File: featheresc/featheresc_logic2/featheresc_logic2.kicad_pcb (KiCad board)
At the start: 2 copper layers, 77 x 39 mm, 52 parts, among them J1 RC IN 1, J2 RC IN 2, J3 soicbite prog connector, J7 Interconnect 1, J8 Interconnect 2, SW1 SW_DIP_x01, U1 AMS1117-50, U2 XL1509-ADJE1, U3 ATtiny1614-SS, U4 NCP81155MN, U5 NCP81155MN, U6 NCP81155MN, U7 NCP81155MN, U8 78L12G-AB3-R

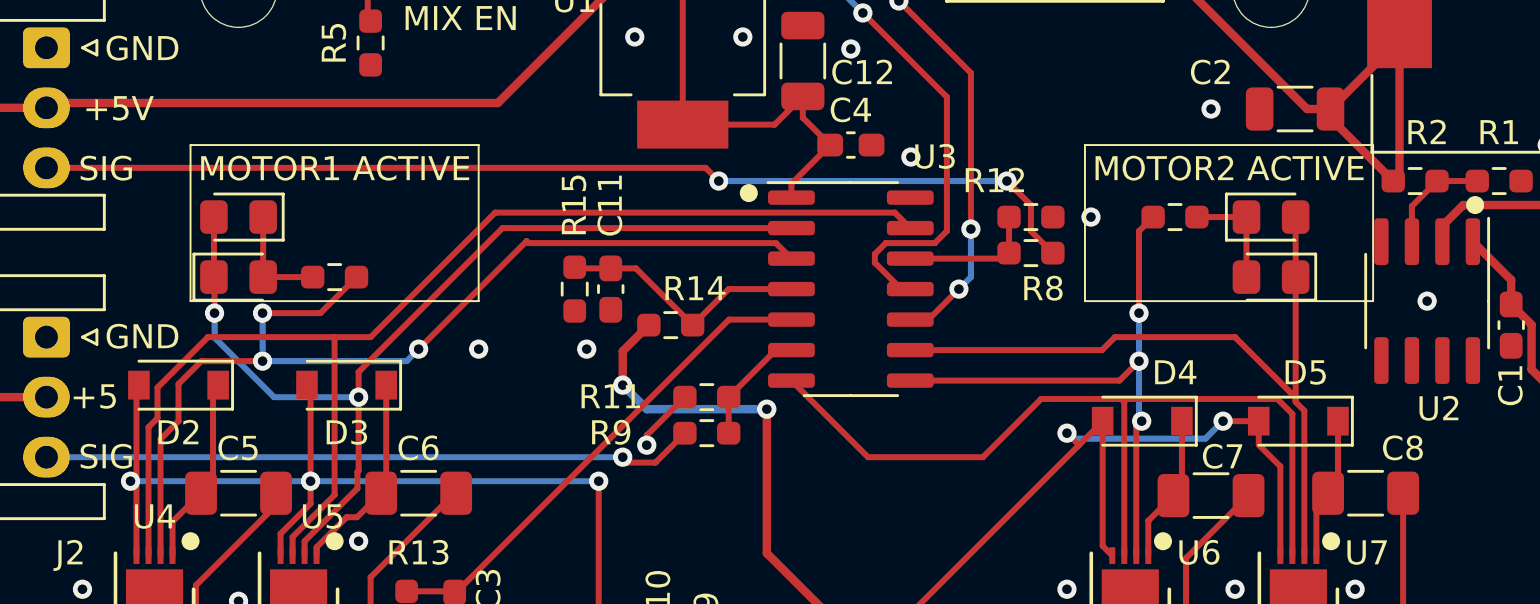
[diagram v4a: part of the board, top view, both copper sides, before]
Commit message: Pulldown EN pins
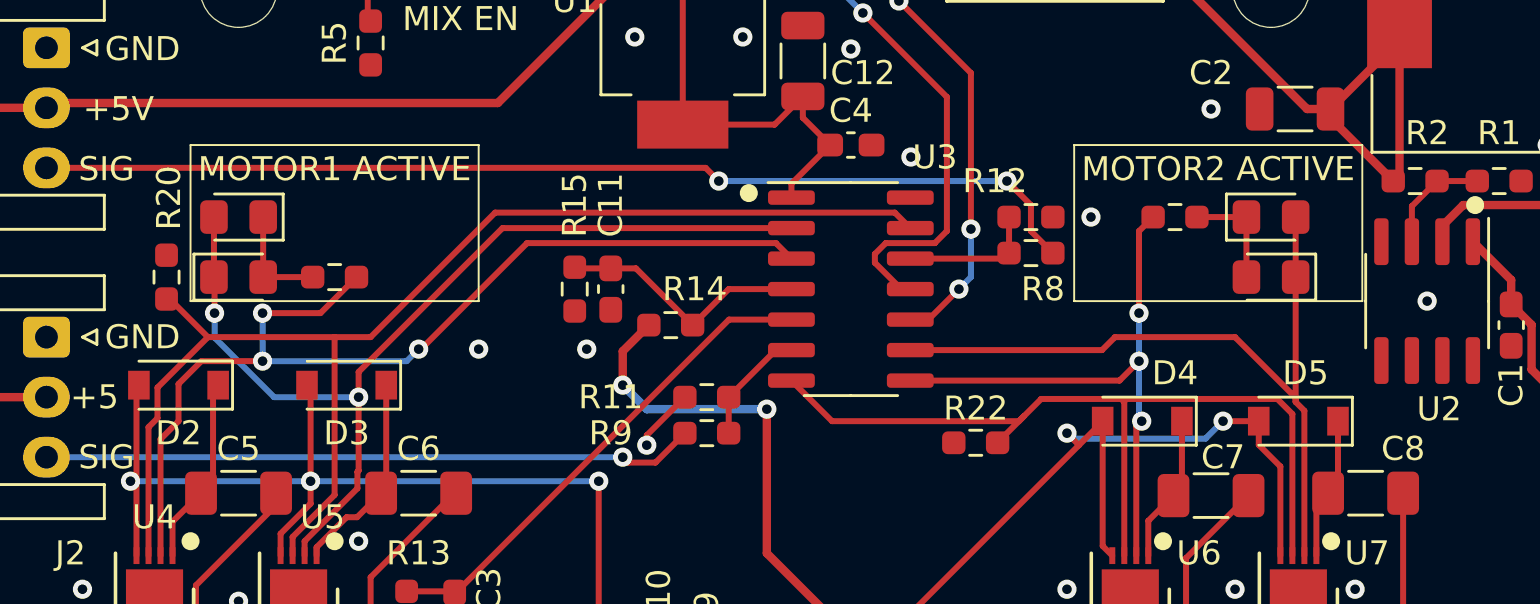
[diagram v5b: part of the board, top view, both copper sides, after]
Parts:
- added R20: 33k, Resistor_SMD:R_0603_1608Metric_Pad0.98x0.95mm_HandSolder, F.Cu at (125.0, 77.0)
- added R22: 33k, Resistor_SMD:R_0603_1608Metric_Pad0.98x0.95mm_HandSolder, F.Cu at (158.7, 83.9)
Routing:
- net /MOTOREN_1: track 51.6 -> 54.0 mm
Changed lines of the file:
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@@
+    )
+  )
+  (footprint "Resistor_SMD:R_0603_1608Metric_Pad0.98x0.95mm_HandSolder" (layer "F.Cu")
+    (at 158.7 83.9)
+    (descr "Resistor SMD 0603 (1608 Metric), square (rectangular) end terminal, IPC_7351 nominal with elongated pad for handsoldering. (Body size source: IPC-SM-782 page 72, https://www.pcb-3d.com/wordpress/wp-content/uploads/ipc-sm-782a_amendment_1_and_2.pdf), generated with kicad-footprint-generator")
+    (tags "resistor handsolder")
+    (property "Sheetfile" "gatedrivers.kicad_sch")
+    (property "Sheetname" "gatedrivers2")
+    (attr smd)
+    (fp_text reference "R22" (at 0 -1.43) (layer "F.SilkS")
+      (effects (font (size 1 1) (thickness 0.15)))
+    )
+    (fp_text value "33k" (at 0 1.43) (layer "F.Fab")
+      (effects (font (size 1 1) (thickness 0.15)))
+    )
+    (fp_text user "${REFERENCE}" (at 0 0) (layer "F.Fab")
+      (effects (font (size 0.4 0.4) (thickness 0.06)))
+    )
+    (fp_line (start -0.254724 0.5225) (end 0.254724 0.5225) (layer "F.SilkS") (width 0.12))
+    (fp_line (start -0.254724 -0.5225) (end 0.254724 -0.5225) (layer "F.SilkS") (width 0.12))
+    (fp_line (start 1.65 0.73) (end -1.65 0.73) (layer "F.CrtYd") (width 0.05))
+    (fp_line (start -1.65 -0.73) (end 1.65 -0.73) (layer "F.CrtYd") (width 0.05))
+    (fp_line (start -1.65 0.73) (end -1.65 -0.73) (layer "F.CrtYd") (width 0.05))
+    (fp_line (start 1.65 -0.73) (end 1.65 0.73) (layer "F.CrtYd") (width 0.05))
+    (fp_line (start -0.8 -0.4125) (end 0.8 -0.4125) (layer "F.Fab") (width 0.1))
+    (fp_line (start 0.8 -0.4125) (end 0.8 0.4125) (layer "F.Fab") (width 0.1))
+    (fp_line (start -0.8 0.4125) (end -0.8 -0.4125) (layer "F.Fab") (width 0.1))
+    (fp_line (start 0.8 0.4125) (end -0.8 0.4125) (layer "F.Fab") (width 0.1))
+    (pad "1" smd roundrect locked (at -0.9125 0) (size 0.975 0.95) (layers "F.Cu" "F.Paste" "F.Mask") (roundrect_rratio 0.25)
+      (net 1 "GND") (pintype "passive"))
+    (pad "2" smd roundrect locked (at 0.9125 0) (size 0.975 0.95) (layers "F.Cu" "F.Paste" "F.Mask") (roundrect_rratio 0.25)
+      (net 41 "/MOTOREN_2") (pintype "passive"))
+    (model "${KICAD6_3DMODEL_DIR}/Resistor_SMD.3dshapes/R_0603_1608Metric.wrl"
+      (offset (xyz 0 0 0))
+      (scale (xyz 1 1 1))
+      (rotate (xyz 0 0 0))
     )
   )
@@
     (pad "8" smd oval (at 1.905 -0.75 180) (size 0.8 1.5) (layers "B.Cu" "B.Mask")
       (net 3 "/TXDEBUG") (pinfunction "Pin_8") (pintype "passive"))
+  )
+  (footprint "Resistor_SMD:R_0603_1608Metric_Pad0.98x0.95mm_HandSolder" (layer "F.Cu")
+    (at 125 77 -90)
+    (descr "Resistor SMD 0603 (1608 Metric), square (rectangular) end terminal, IPC_7351 nominal with elongated pad for handsoldering. (Body size source: IPC-SM-782 page 72, https://www.pcb-3d.com/wordpress/wp-content/uploads/ipc-sm-782a_amendment_1_and_2.pdf), generated with kicad-footprint-generator")
+    (tags "resistor handsolder")
+    (property "Sheetfile" "gatedrivers.kicad_sch")
+    (property "Sheetname" "gatedrivers1")
+    (attr smd)
+    (fp_text reference "R20" (at -3.3 -0.1 90) (layer "F.SilkS")
+      (effects (font (size 1 1) (thickness 0.15)))
+    )
+    (fp_text value "33k" (at 0 1.43 90) (layer "F.Fab")
+      (effects (font (size 1 1) (thickness 0.15)))
+    )
+    (fp_text user "${REFERENCE}" (at 0 0 90) (layer "F.Fab")
+      (effects (font (size 0.4 0.4) (thickness 0.06)))
+    )
+    (fp_line (start -0.254724 0.5225) (end 0.254724 0.5225) (layer "F.SilkS") (width 0.12))
+    (fp_line (start -0.254724 -0.5225) (end 0.254724 -0.5225) (layer "F.SilkS") (width 0.12))
+    (fp_line (start 1.65 -0.73) (end 1.65 0.73) (layer "F.CrtYd") (width 0.05))
+    (fp_line (start -1.65 0.73) (end -1.65 -0.73) (layer "F.CrtYd") (width 0.05))
+    (fp_line (start -1.65 -0.73) (end 1.65 -0.73) (layer "F.CrtYd") (width 0.05))
+    (fp_line (start 1.65 0.73) (end -1.65 0.73) (layer "F.CrtYd") (width 0.05))
+    (fp_line (start 0.8 -0.4125) (end 0.8 0.4125) (layer "F.Fab") (width 0.1))
+    (fp_line (start -0.8 -0.4125) (end 0.8 -0.4125) (layer "F.Fab") (width 0.1))
+    (fp_line (start -0.8 0.4125) (end -0.8 -0.4125) (layer "F.Fab") (width 0.1))
+    (fp_line (start 0.8 0.4125) (end -0.8 0.4125) (layer "F.Fab") (width 0.1))
+    (pad "1" smd roundrect locked (at -0.9125 0 270) (size 0.975 0.95) (layers "F.Cu" "F.Paste" "F.Mask") (roundrect_rratio 0.25)
+      (net 1 "GND") (pintype "passive"))
+    (pad "2" smd roundrect locked (at 0.9125 0 270) (size 0.975 0.95) (layers "F.Cu" "F.Paste" "F.Mask") (roundrect_rratio 0.25)
+      (net 38 "/MOTOREN_1") (pintype "passive"))
+    (model "${KICAD6_3DMODEL_DIR}/Resistor_SMD.3dshapes/R_0603_1608Metric.wrl"
+      (offset (xyz 0 0 0))
+      (scale (xyz 1 1 1))
+      (rotate (xyz 0 0 0))
+    )
   )
   (footprint "Package_DFN_QFN:DFN-8-1EP_3x3mm_P0.5mm_EP1.66x2.38mm" (layer "F.Cu")
@@
   (gr_rect (start 126 71.5) (end 138 78) (layer "F.SilkS") (width 0.08) (fill none))
   (gr_circle (center 166.5 88) (end 166.8 88) (layer "F.SilkS") (width 0.15) (fill solid))
-  (gr_rect (start 163.25 71.5) (end 175.25 78) (layer "F.SilkS") (width 0.08) (fill none))
+  (gr_rect (start 162.8 71.5) (end 174.8 78) (layer "F.SilkS") (width 0.08) (fill none))
   (gr_line (start 157.5 61) (end 157.5 65.5) (layer "F.SilkS") (width 0.15))
   (gr_line (start 171 55) (end 171 104) (layer "Dwgs.User") (width 0.15))
@@
     (effects (font (size 1 1) (thickness 0.15)))
   )
-  (gr_text "MOTOR2 ACTIVE" (at 169.25 72.5) (layer "F.SilkS")
+  (gr_text "MOTOR2 ACTIVE" (at 168.8 72.5) (layer "F.SilkS")
     (effects (font (size 1 1) (thickness 0.15)))
   )
@@
   (segment (start 129.475386 82) (end 127 79.524614) (width 0.25) (layer "B.Cu") (net 36))
   (segment (start 127 79.524614) (end 127 78.5) (width 0.25) (layer "B.Cu") (net 36))
+  (segment (start 135.5 80) (end 135.6 80) (width 0.25) (layer "F.Cu") (net 37))
+  (segment (start 150.37952 75.58452) (end 151.025 76.23) (width 0.25) (layer "F.Cu") (net 37))
   (segment (start 126.450978 80.5) (end 129 80.5) (width 0.25) (layer "F.Cu") (net 37))
   (segment (start 129 78.5) (end 131.4125 78.5) (width 0.25) (layer "F.Cu") (net 37))
   (segment (start 125.5 81.450978) (end 126.450978 80.5) (width 0.25) (layer "F.Cu") (net 37))
   (segment (start 125.5 83) (end 125.5 81.450978) (width 0.25) (layer "F.Cu") (net 37))
+  (segment (start 135.6 80) (end 140.01548 75.58452) (width 0.25) (layer "F.Cu") (net 37))
   (segment (start 124.75 83.75) (end 125.5 83) (width 0.25) (layer "F.Cu") (net 37))
-  (segment (start 150.37952 75.58452) (end 151.025 76.23) (width 0.25) (layer "F.Cu") (net 37))
-  (segment (start 135.5 80) (end 140 75.5) (width 0.25) (layer "F.Cu") (net 37))
+  (segment (start 140.01548 75.58452) (end 150.37952 75.58452) (width 0.25) (layer "F.Cu") (net 37))
   (segment (start 131.4125 78.5) (end 132.9125 77) (width 0.25) (layer "F.Cu") (net 37))
-  (segment (start 140.08452 75.58452) (end 150.37952 75.58452) (width 0.25) (layer "F.Cu") (net 37))
-  (segment (start 140 75.5) (end 140.08452 75.58452) (width 0.25) (layer "F.Cu") (net 37))
   (segment (start 124.75 88.6) (end 124.75 83.75) (width 0.25) (layer "F.Cu") (net 37))
   (via (at 129 80.5) (size 0.8) (drill 0.4) (layers "F.Cu" "B.Cu") (net 37))
@@
   (segment (start 155.32952 74.31452) (end 155.975 74.96) (width 0.25) (layer "F.Cu") (net 38))
   (segment (start 132 79.5) (end 126.725489 79.5) (width 0.25) (layer "F.Cu") (net 38))
+  (segment (start 125.137989 77.9125) (end 126.725489 79.5) (width 0.25) (layer "F.Cu") (net 38))
   (segment (start 130.25 87.82321) (end 132 86.07321) (width 0.25) (layer "F.Cu") (net 38))
+  (segment (start 125 77.9125) (end 125.137989 77.9125) (width 0.25) (layer "F.Cu") (net 38))
   (segment (start 133.5 79.5) (end 138.68548 74.31452) (width 0.25) (layer "F.Cu") (net 38))
   (segment (start 132 79.5) (end 133.5 79.5) (width 0.25) (layer "F.Cu") (net 38))
@@
   (segment (start 164.5 79.5) (end 169.5 79.5) (width 0.25) (layer "F.Cu") (net 40))
   (segment (start 172.025 82.025) (end 172.025 82.20276) (width 0.25) (layer "F.Cu") (net 40))
-  (segment (start 159 84.5) (end 154.215 84.5) (width 0.25) (layer "F.Cu") (net 41))
   (segment (start 164.762011 82.075489) (end 161.424511 82.075489) (width 0.25) (layer "F.Cu") (net 41))
+  (segment (start 160.5 83) (end 152.715 83) (width 0.25) (layer "F.Cu") (net 41))
+  (segment (start 152.715 83) (end 151.025 81.31) (width 0.25) (layer "F.Cu") (net 41))
   (segment (start 171.262011 82.075489) (end 164.762011 82.075489) (width 0.25) (layer "F.Cu") (net 41))
-  (segment (start 154.215 84.5) (end 151.025 81.31) (width 0.25) (layer "F.Cu") (net 41))
+  (segment (start 159.6125 83.9) (end 159.6125 83.8875) (width 0.25) (layer "F.Cu") (net 41))
   (segment (start 164.8875 82.200978) (end 164.762011 82.075489) (width 0.25) (layer "F.Cu") (net 41))
-  (segment (start 161.424511 82.075489) (end 159 84.5) (width 0.25) (layer "F.Cu") (net 41))
+  (segment (start 159.6125 83.8875) (end 160.7 82.8) (width 0.25) (layer "F.Cu") (net 41))
   (segment (start 171.8875 82.700978) (end 171.262011 82.075489) (width 0.25) (layer "F.Cu") (net 41))
   (segment (start 171.8875 88.6) (end 171.8875 82.700978) (width 0.25) (layer "F.Cu") (net 41))
+  (segment (start 161.424511 82.075489) (end 160.7 82.8) (width 0.25) (layer "F.Cu") (net 41))
+  (segment (start 160.7 82.8) (end 160.5 83) (width 0.25) (layer "F.Cu") (net 41))
   (segment (start 164.8875 88.6) (end 164.8875 82.200978) (width 0.25) (layer "F.Cu") (net 41))
   (segment (start 178.135 75.525) (end 178.135 74.865) (width 0.35) (layer "F.Cu") (net 42))

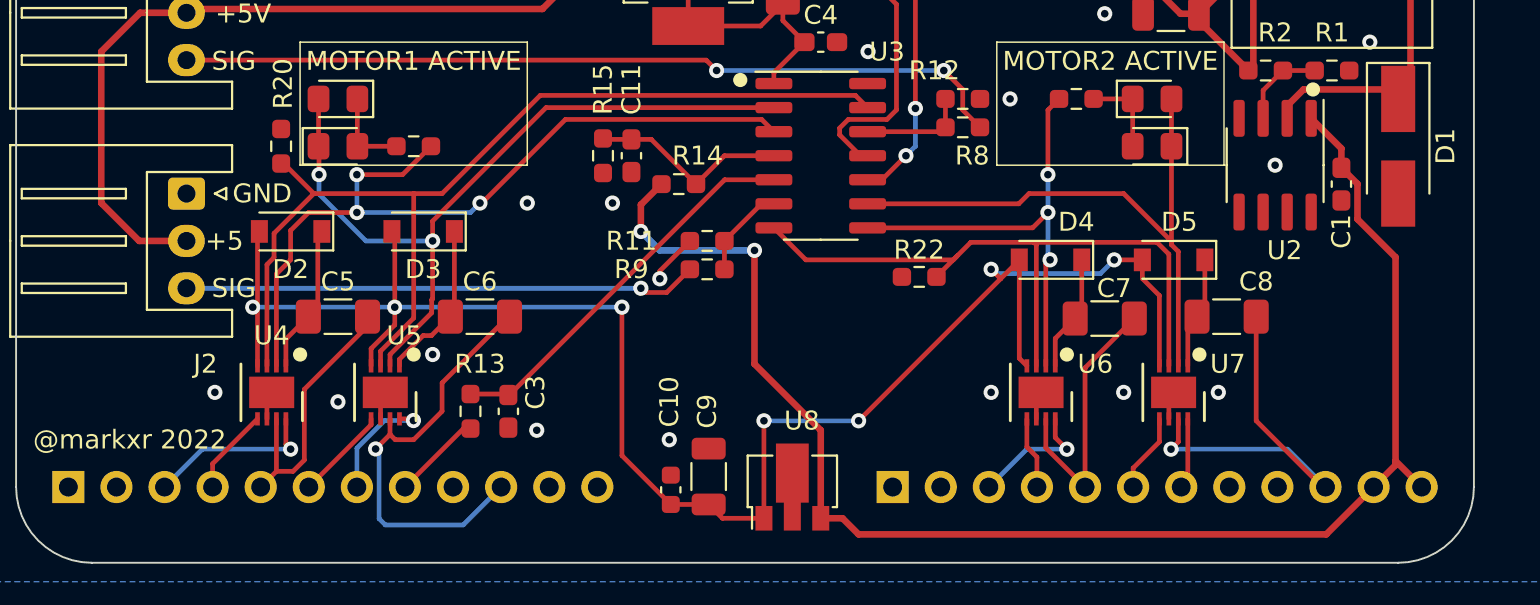
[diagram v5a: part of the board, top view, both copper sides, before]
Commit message: Featheresc logic: add more decoupling caps etc
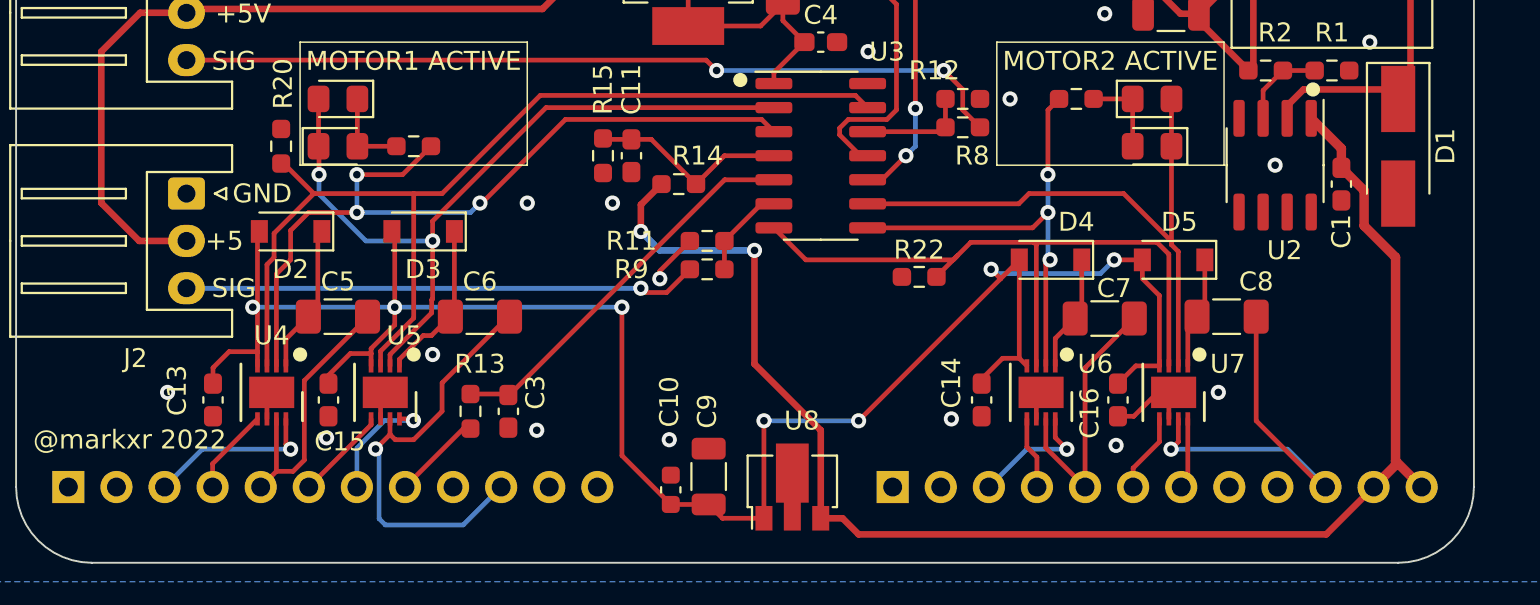
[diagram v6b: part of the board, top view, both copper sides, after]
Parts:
- added C13: 100 nF, Capacitor_SMD:C_0603_1608Metric_Pad1.08x0.95mm_HandSolder, F.Cu at (121.4, 90.4)
- added C14: 100 nF, Capacitor_SMD:C_0603_1608Metric_Pad1.08x0.95mm_HandSolder, F.Cu at (162.0, 90.4)
- added C15: 100 nF, Capacitor_SMD:C_0603_1608Metric_Pad1.08x0.95mm_HandSolder, F.Cu at (127.5, 90.4)
- added C16: 100 nF, Capacitor_SMD:C_0603_1608Metric_Pad1.08x0.95mm_HandSolder, F.Cu at (169.2, 90.4)
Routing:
- net +12V: track 94.0 -> 106.0 mm
- net GND: track 11.1 -> 14.5 mm
